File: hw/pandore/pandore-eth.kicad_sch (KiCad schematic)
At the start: 0 parts

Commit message: added RP2350's crystals added 8p8c shielded with led connector (both the same for now)
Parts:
- added J1: 8p8c_2led_shield, reekilib_con:amphenol_RJE58-188-54x1-0x, symbol reekilib_con:8p8c_2led_shield
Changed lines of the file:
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@@
 		(company "${corp}")
 	)
+	(symbol
+		(lib_id "reekilib_con:8p8c_2led_shield")
+		(at 254 52.07 0)
+		(mirror y)
+		(unit 1)
+		(exclude_from_sim no)
+		(in_bom yes)
+		(on_board yes)
+		(dnp no)
+		(fields_autoplaced yes)
+		(property "Reference" "J1"
+			(at 254 36.83 0)
+			(do_not_autoplace yes)
+			(effects
+				(font
+					(size 1 1)
+				)
+			)
+		)
+		(property "Value" "8p8c_2led_shield"
+			(at 261.62 52.07 90)
+			(do_not_autoplace yes)
+			(effects
+				(font
+					(size 1 1)
+				)
+			)
+		)
+		(property "Footprint" "reekilib_con:amphenol_RJE58-188-54x1-0x"
+			(at 254 80.645 0)
+			(do_not_autoplace yes)
+			(effects
+				(font
+					(size 1 1)
+				)
+				(hide yes)
+			)
+		)
+		(property "Datasheet" "https://cdn.amphenol-cs.com/media/wysiwyg/files/drawing/rje581885xx1.pdf"
+			(at 254 83.185 0)
+			(do_not_autoplace yes)
+			(effects
+				(font
+					(size 1 1)
+				)
+				(hide yes)
+			)
+		)
+		(property "Description" "8P8C Ethernet connector, 2LED with shield"
+			(at 254 81.915 0)
+			(do_not_autoplace yes)
+			(effects
+				(font
+					(size 1 1)
+				)
+				(hide yes)
+			)
+		)
+		(property "Vmax" "125V"
+			(at 257.81 77.47 0)
+			(do_not_autoplace yes)
+			(effects
+				(font
+					(size 1 1)
+				)
+				(justify right)
+				(hide yes)
+			)
+		)
+		(property "Imax" "1.25A"
+			(at 254 77.47 0)
+			(do_not_autoplace yes)
+			(effects
+				(font
+					(size 1 1)
+				)
+				(hide yes)
+			)
+		)
+		(property "MPN" "RJE581885411"
+			(at 254 87.63 0)
+			(do_not_autoplace yes)
+			(effects
+				(font
+					(size 1 1)
+				)
+				(hide yes)
+			)
+		)
+		(property "MFG" "Amphenol ICC (Commercial Products)"
+			(at 241.3 87.63 0)
+			(do_not_autoplace yes)
+			(effects
+				(font
+					(size 1 1)
+				)
+				(justify left)
+				(hide yes)
+			)
+		)
+		(property "Link" "https://www.amphenol-cs.com/product/rje581885411.html"
+			(at 203.2 87.63 0)
+			(do_not_autoplace yes)
+			(effects
+				(font
+					(size 1 1)
+				)
+				(justify left)
+				(hide yes)
+			)
+		)
+		(pin "CL"
+		)
+		(pin "3"
+		)
+		(pin "SH"
+		)
+		(pin "AL"
+		)
+		(pin "4"
+		)
+		(pin "5"
+		)
+		(pin "6"
+		)
+		(pin "AR"
+		)
+		(pin "2"
+		)
+		(pin "CR"
+		)
+		(pin "1"
+		)
+		(pin "7"
+		)
+		(pin "8"
+		)
+		(instances
+			(project ""
+				(path "/e55f2700-f75a-4062-8a27-fe258faa8966/83546ca1-08e2-4cd0-99ad-1e2a6bc1b076"
+					(reference "J2")
+					(unit 1)
+				)
+				(path "/e55f2700-f75a-4062-8a27-fe258faa8966/b69294f0-a26d-445f-ba7c-20a0f29876f9"
+					(reference "J1")
+					(unit 1)
+				)
+			)
+		)
+	)
 )

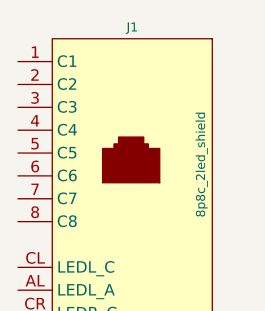
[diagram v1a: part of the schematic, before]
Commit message: added all remaining connectors (only missing M.2 now)
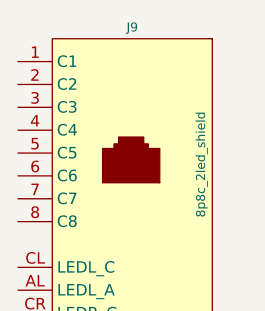
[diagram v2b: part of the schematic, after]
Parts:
- renumbered J1 to J9
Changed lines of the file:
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@@
 		(dnp no)
 		(fields_autoplaced yes)
-		(property "Reference" "J1"
+		(property "Reference" "J9"
 			(at 254 36.83 0)
 			(do_not_autoplace yes)
@@
 			(project ""
 				(path "/e55f2700-f75a-4062-8a27-fe258faa8966/83546ca1-08e2-4cd0-99ad-1e2a6bc1b076"
-					(reference "J2")
+					(reference "J8")
 					(unit 1)
 				)
 				(path "/e55f2700-f75a-4062-8a27-fe258faa8966/b69294f0-a26d-445f-ba7c-20a0f29876f9"
-					(reference "J1")
+					(reference "J9")
 					(unit 1)
 				)

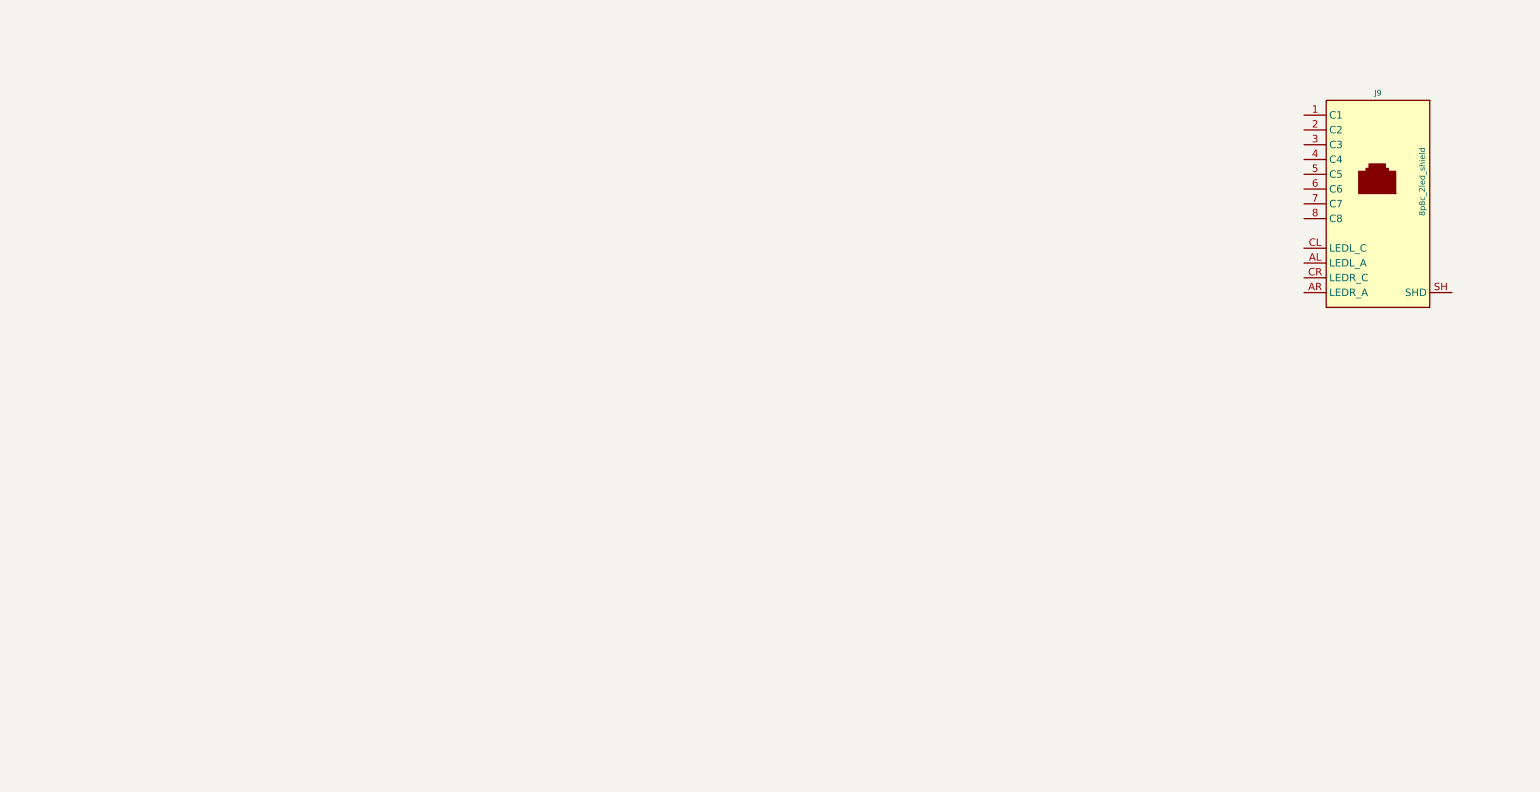
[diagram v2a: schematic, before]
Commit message: Added lots to sch and pcb: eth passive, audio codec, midi, teensy Corrected and added support for M.2
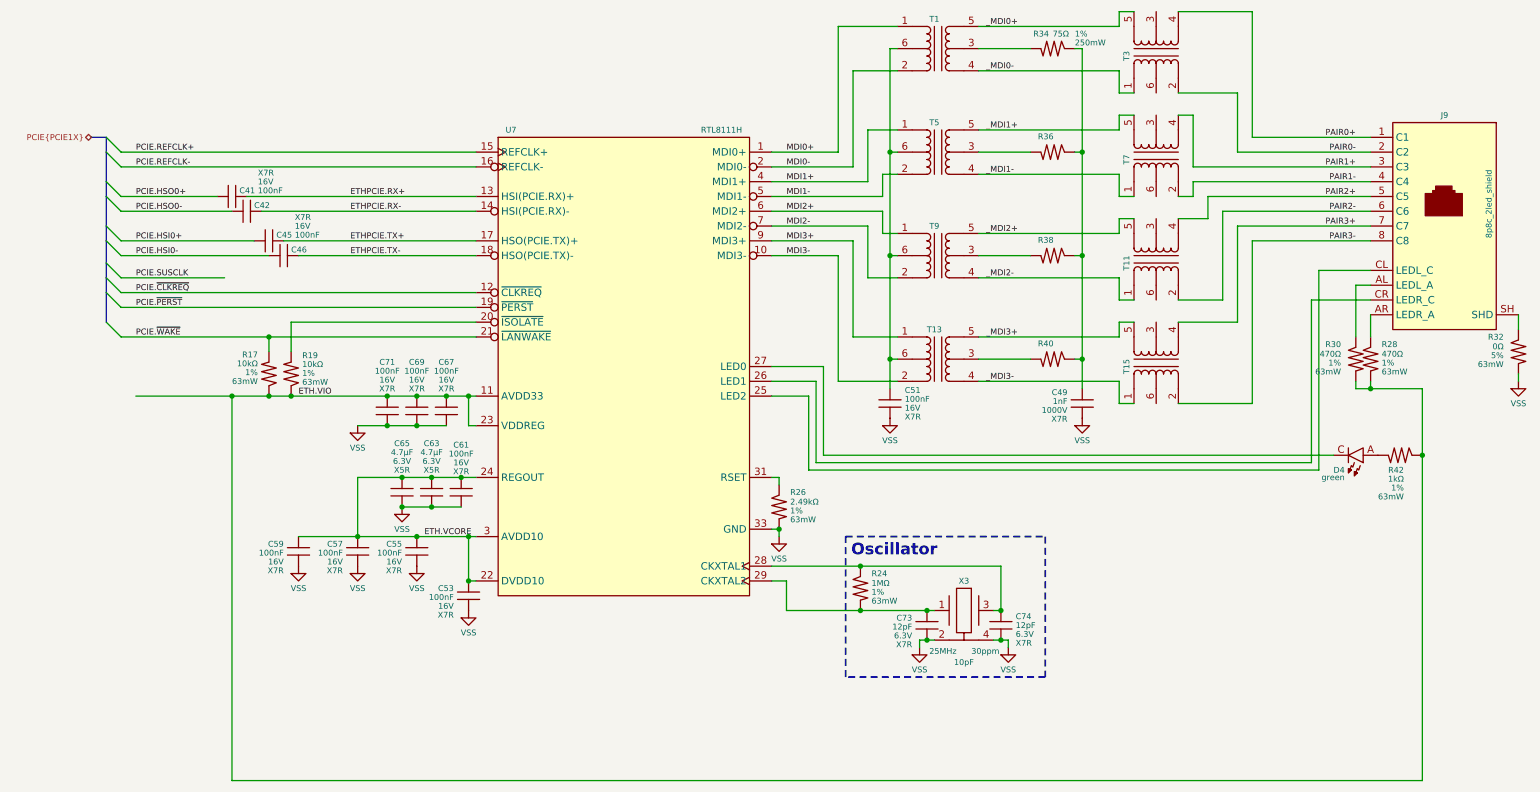
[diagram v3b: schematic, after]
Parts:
- added C41, C42, C45, C46, C51, C53, C55, C57, C59, C61, C63, C65, C67, C69, C71, C73, C74: ${Capacitance}, ${Voltage}, ${Dielectric}, reekilib_cap:CAPC1005, symbol reekilib_cap:cap
- added C49: ${Capacitance}, ${Voltage}, ${Dielectric}, reekilib_cap:CAPC3216, symbol reekilib_cap:cap
- added D4: ${color}, reekilib_led:LEDM1608X80, symbol reekilib_led:led
- added R17, R19, R24, R26, R28, R30, R32, R42: ${Resistance}, ${Tolerance}, ${Power}, reekilib_res:RESC1005, symbol reekilib_res:res
- added R34, R36, R38, R40: ${Resistance}, ${Tolerance}, ${Power}, reekilib_res:RESMELF0204, symbol reekilib_res:res
- added T1, T11, T13, T15, T3, T5, T7, T9: tran_choke_center, reekilib_trf:TDK_ALT3232M, symbol reekilib_trf:tran_choke_center
- added U7: RTL8111H, reekilib_qfn:QFN40P400X400-33, symbol reekilib_trx:RTL8111H
- added X3: ${F}, ${tol}+${stab}, ${load}, reekilib_osc:OSCCC320X250X90, symbol reekilib_xtl:crystal_shield
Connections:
- net PAIR0+: now reaches J9.1 (C1)
- net PAIR0+: now also T3.4
- net PAIR0-: now reaches J9.2 (C2)
- net PAIR0-: now also T3.2
- net PAIR1+: now reaches J9.3 (C3)
- net PAIR1+: now also T7.4
- net PAIR1-: now reaches J9.4 (C4)
- net PAIR1-: now also T7.2
- net PAIR2+: now reaches J9.5 (C5)
- net PAIR2+: now also T11.4
- net PAIR2-: now reaches J9.6 (C6)
- net PAIR2-: now also T11.2
- net PAIR3+: now reaches J9.7 (C7)
- net PAIR3+: now also T15.4
- net PAIR3-: now reaches J9.8 (C8)
- net PAIR3-: now also T15.2
- net at J9.AL (LEDL_A): now also R30.2
- net at J9.AR (LEDR_A): now also R28.2
- net at J9.CL (LEDL_C): now also U7.25 (LED2)
- net at J9.CR (LEDR_C): now also U7.26 (LED1)
- net at J9.SH (SHD): now also R32.2
- new net: R38.1, T9.3
- new net: C49.2, R34.2, R36.2, R38.2, R40.2
- new net: R36.1, T5.3
- new net: R40.1, T13.3
- new net: R34.1, T1.3
- new net: C51.2, T1.6, T13.6, T5.6, T9.6
- new net: C73.2, R24.1, U7.29 (CKXTAL2), X3.1
- new net: R19.1, U7.20 (~{ISOLATE})
- new net: D4.C, U7.27 (LED0)
- new net: C74.2, R24.2, U7.28 (CKXTAL1), X3.3
- new net: R26.2, U7.31 (RSET)
- new net: D4.A, R42.1
- new net ETH.VCORE: C53.2, C55.2, C57.2, C59.2, C61.2, C63.2, C65.2, U7.22 (DVDD10), U7.24 (REGOUT), U7.3 (AVDD10), U7.30 (AVDD10), U7.8 (AVDD10)
- new net ETH.VIO: C67.2, C69.2, C71.2, R17.2, R19.2, R28.1, R30.1, R42.2, U7.11 (AVDD33), U7.23 (VDDREG), U7.32 (AVDD33)
- new net ETHPCIE.RX+: C41.1, U7.13 (HSI(PCIE.RX)+)
- new net ETHPCIE.RX-: C42.1, U7.14 (HSI(PCIE.RX)-)
- new net ETHPCIE.TX+: C45.1, U7.17 (HSO(PCIE.TX)+)
- new net ETHPCIE.TX-: C46.1, U7.18 (HSO(PCIE.TX)-)
- new net MDI0+: T1.1, U7.1 (MDI0+)
- new net MDI0-: T1.2, U7.2 (MDI0-)
- new net MDI1+: T5.1, U7.4 (MDI1+)
- new net MDI1-: T5.2, U7.5 (MDI1-)
- new net MDI2+: T9.1, U7.6 (MDI2+)
- new net MDI2-: T9.2, U7.7 (MDI2-)
- new net MDI3+: T13.1, U7.9 (MDI3+)
- new net MDI3-: T13.2, U7.10 (MDI3-)
- new net PCIE.HSI0+: C45.2
- new net PCIE.HSI0-: C46.2
- new net PCIE.HSO0+: C41.2
- new net PCIE.HSO0-: C42.2
- new net PCIE.REFCLK+: U7.15 (REFCLK+)
- new net PCIE.REFCLK-: U7.16 (REFCLK-)
- new net PCIE.~{CLKREQ}: U7.12 (~{CLKREQ})
- new net PCIE.~{PERST}: U7.19 (~{PERST})
- new net PCIE.~{WAKE}: R17.1, U7.21 (~{LANWAKE})
- new net VSS: C49.1, C51.1, C53.1, C55.1, C57.1, C59.1, C61.1, C63.1, C65.1, C67.1, C69.1, C71.1, C73.1, C74.1, R26.1, R32.1, U7.33 (GND), X3.2, X3.4
- new net _MDI0+: T1.5, T3.5
- new net _MDI0-: T1.4, T3.1
- new net _MDI1+: T5.5, T7.5
- new net _MDI1-: T5.4, T7.1
- new net _MDI2+: T11.5, T9.5
- new net _MDI2-: T11.1, T9.4
- new net _MDI3+: T13.5, T15.5
- new net _MDI3-: T13.4, T15.1
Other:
- moved on the sheet: J9

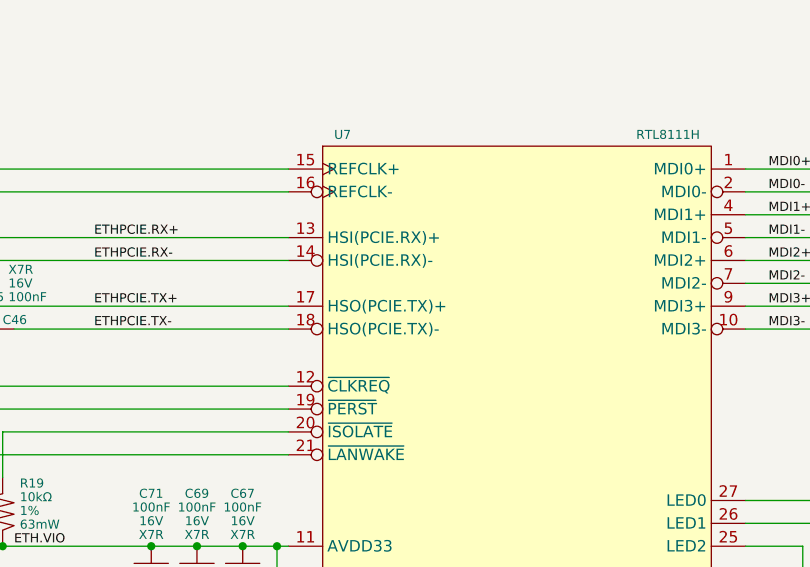
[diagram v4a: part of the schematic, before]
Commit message: most of board control signals added, routed and defined
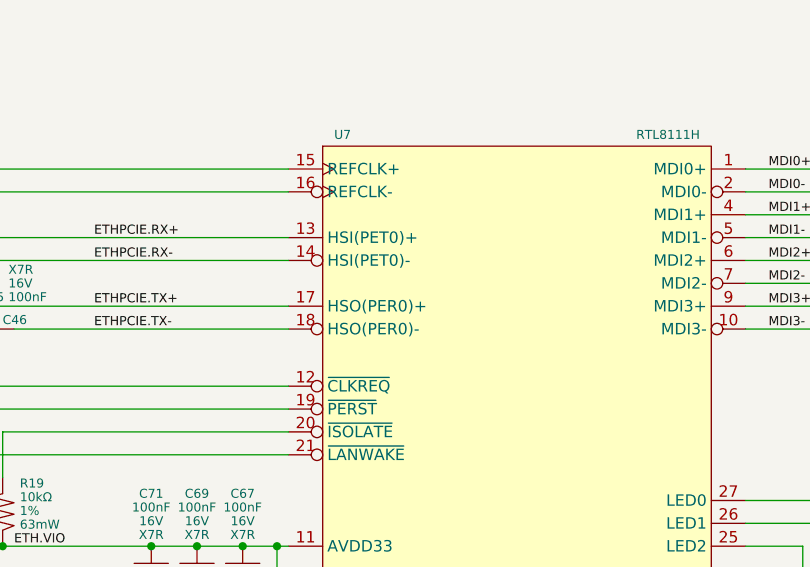
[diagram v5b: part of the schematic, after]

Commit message: last sprint almost done, most routing done
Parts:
- removed R17: ${Resistance}, ${Tolerance}, ${Power}, reekilib_res:RESC1005, symbol reekilib_res:res
- removed T1, T11, T13, T15, T3, T5, T7, T9: tran_choke_center, reekilib_trf:TDK_ALT3232M, symbol reekilib_trf:tran_choke_center
- added T1: trans_pulse_4, reekilib_trf:WE_749020111A, symbol reekilib_trf:trans_pulse_4
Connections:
- net MDI0+: now also T1.12 (RD-)
- net MDI0-: now also T1.11 (RD+)
- net MDI1+: now also T1.8 (TD-)
- net MDI1-: now also T1.7 (TD+)
- net MDI2+: now also T1.6 (RD-)
- net MDI2-: now also T1.5 (RD+)
- net MDI3+: now also T1.2 (TD-)
- net MDI3-: now also T1.1 (TD+)
- net PAIR0+: now also T1.13 (RX-)
- net PAIR0-: now also T1.14 (RX+)
- net PAIR1+: now also T1.17 (TX-)
- net PAIR1-: now also T1.18 (TX+)
- net PAIR2+: now also T1.19 (RX-)
- net PAIR2-: now also T1.20 (RX+)
- net PAIR3+: now also T1.23 (TX-)
- net PAIR3-: now also T1.24 (TX+)
- net at R38.1: now also T1.21 (RXCT)
- net at R36.1: now also T1.16 (TXCT)
- net at R40.1: now also T1.22 (TXCT)
- net at R34.1: now also T1.15 (RXCT)
- net at C51.2: now also T1.10 (RCT), T1.3 (TCT), T1.4 (RCT), T1.9 (TCT)
- net ETH.VIO renamed V3P3
- net PCIE.~{PERST} renamed PWRON
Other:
- moved on the sheet: C49, R34, R36, R38, R40

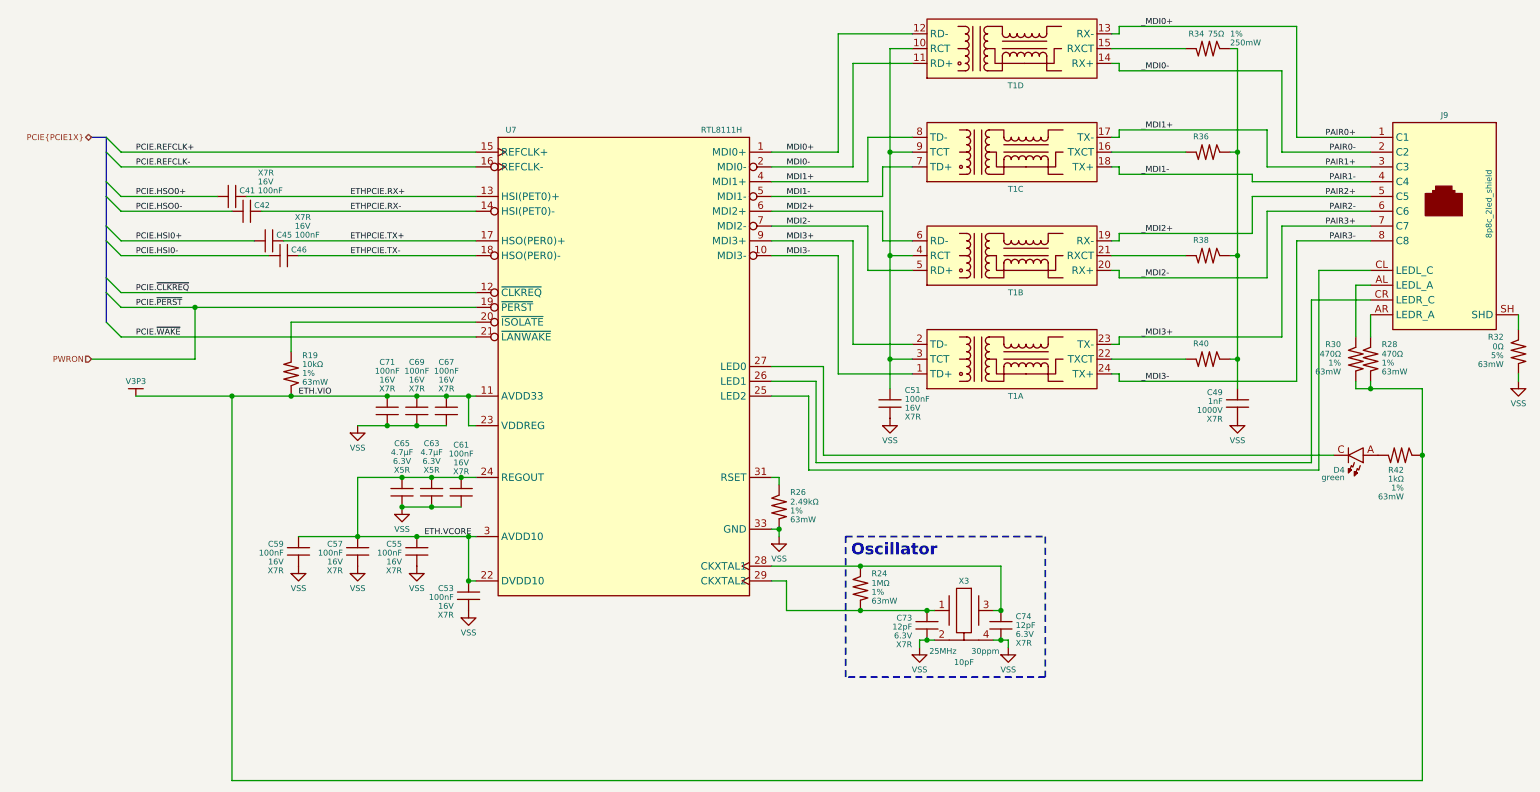
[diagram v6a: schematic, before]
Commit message: finished adding mpn,mfg to all parts, finished routing placement
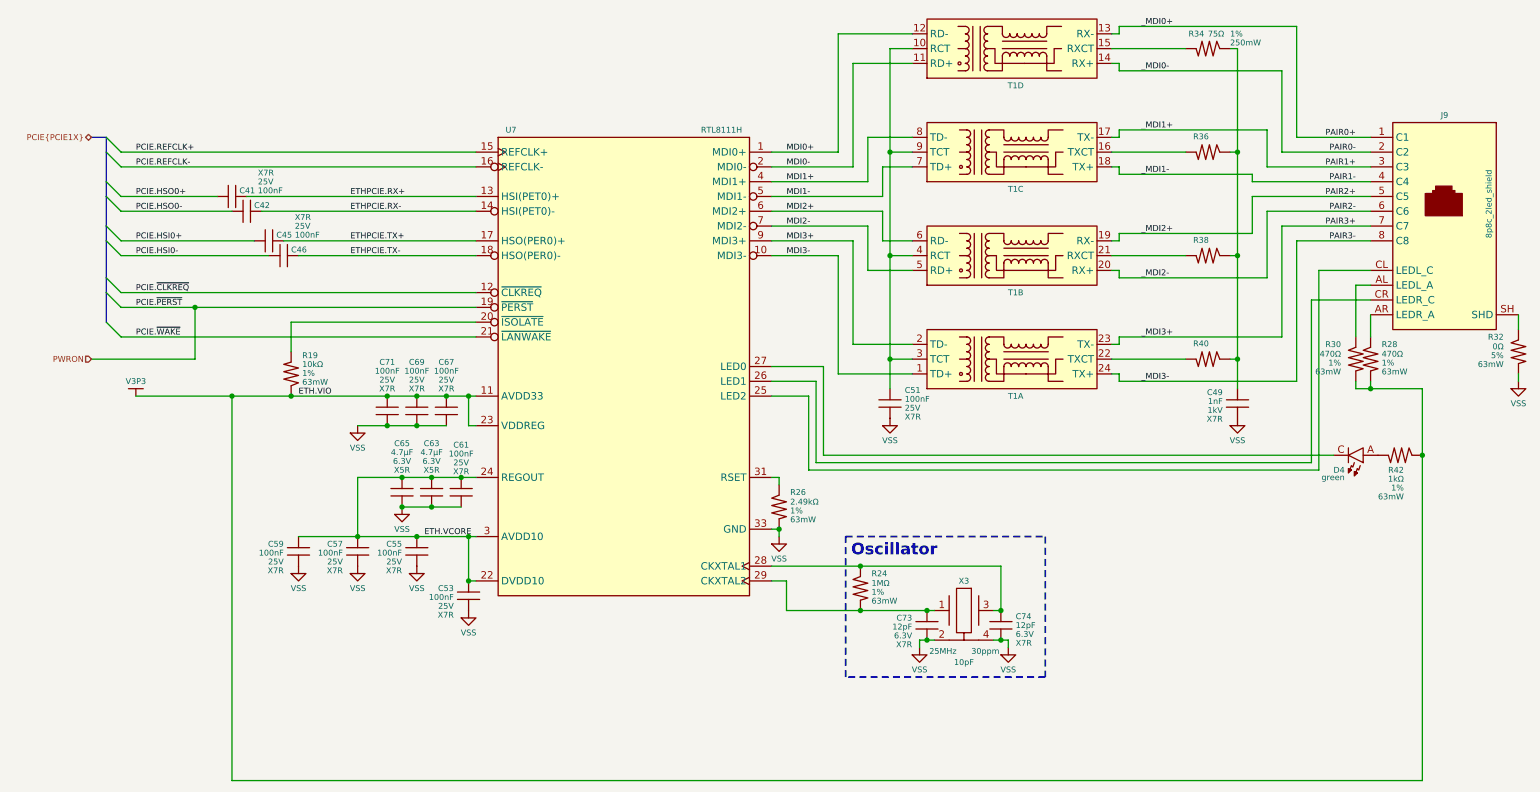
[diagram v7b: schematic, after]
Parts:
- C41, C42, C45, C46, C51, C53, C55, C57, C59, C61, C67, C69, C71: MFG2 Samsung Electro-Mechanics -> (none); MFG3 Taiyo Yuden -> (none); MPN2 CL05B104KA5NNNC -> (none); MPN3 EMK105B7104KV-F -> (none); Voltage 16V -> 25V
- C49: MFG (none) -> Johanson Dielectrics Inc.; MPN (none) -> VPDD202W102K1GV001E; Voltage 1000V -> 1kV
- C73, C74: Link (none) -> https://yageogroup.com/products/Capacitors/part/CC0402JRNPO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; MFG (none) -> Yageo; MPN (none) -> CC0402JRNPO9BN120
- R24: Link (none) -> https://yageogroup.com/products/Resistors/part/RC0402FR-071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; MFG (none) -> YAGEO; MPN (none) -> RC0402FR-071ML
- R26: Link (none) -> https://yageogroup.com/products/Resistors/part/RC0402FR-132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; MFG (none) -> YAGEO; MPN (none) -> RC0402FR-132K49L
- R28, R30: Link (none) -> https://yageogroup.com/products/Resistors/part/RC0402FR-074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; MFG (none) -> YAGEO; MPN (none) -> RC0402FR-07470RL
- R32: Link (none) -> https://yageogroup.com/products/Resistors/part/RC0402JR-070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; MFG (none) -> Yageo; MFG2 (none) -> Stackpole; MFG3 (none) -> Vishay Dale; MPN (none) -> RC0402JR-070RL; MPN2 (none) -> RMCF0402ZT0R00; MPN3 (none) -> CRCW04020000Z0ED
- R42: Link (none) -> https://yageogroup.com/products/Resistors/part/RC0402FR-131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; MFG (none) -> YAGEO; MPN (none) -> RC0402FR-131KL
- X3: MFG (none) -> Abracon LLC; MPN (none) -> ABM8G-25.000MHZ-B4Y-T
